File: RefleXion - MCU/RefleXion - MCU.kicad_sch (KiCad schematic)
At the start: 22 parts, among them J1 Conn_01x21, J2 USB_C_Receptacle_USB2.0, J3 Conn_01x01, J4 Conn_01x01, J5 Conn_01x21, J6 USB_C_Receptacle_USB2.0, Q1 AO3401A, U1 WeAct_Blackpill_v3_safepin, U2 SRV05-4, U3 74AHCT1G125

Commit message: fixes to RGB
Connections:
- no-connect marks 17 -> 19
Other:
- note added: "Left hand = R1 Right Hand = R2"
- note added: "RGB needs to be b9!"
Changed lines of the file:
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@@
   (no_connect (at 92.71 226.06))
   (no_connect (at 92.71 218.44))
+  (no_connect (at 191.77 245.11))
+  (no_connect (at 191.77 242.57))
   (wire (pts (xy 326.39 205.74) (xy 326.39 207.01))
     (stroke (width 0) (type default) (color 0 0 0 0))
@@
     (stroke (width 0) (type default) (color 0 0 0 0))
   )
+  (text "RGB needs to be b9!\n" (at 161.29 266.7 0)
+    (effects (font (size 1.27 1.27)) (justify left bottom))
+  )
+  (text "Left hand = R1\nRight Hand = R2" (at 337.82 201.93 0)
+    (effects (font (size 1.27 1.27)) (justify left bottom))
+  )
   (label "VBUS2" (at 118.11 213.36 0)

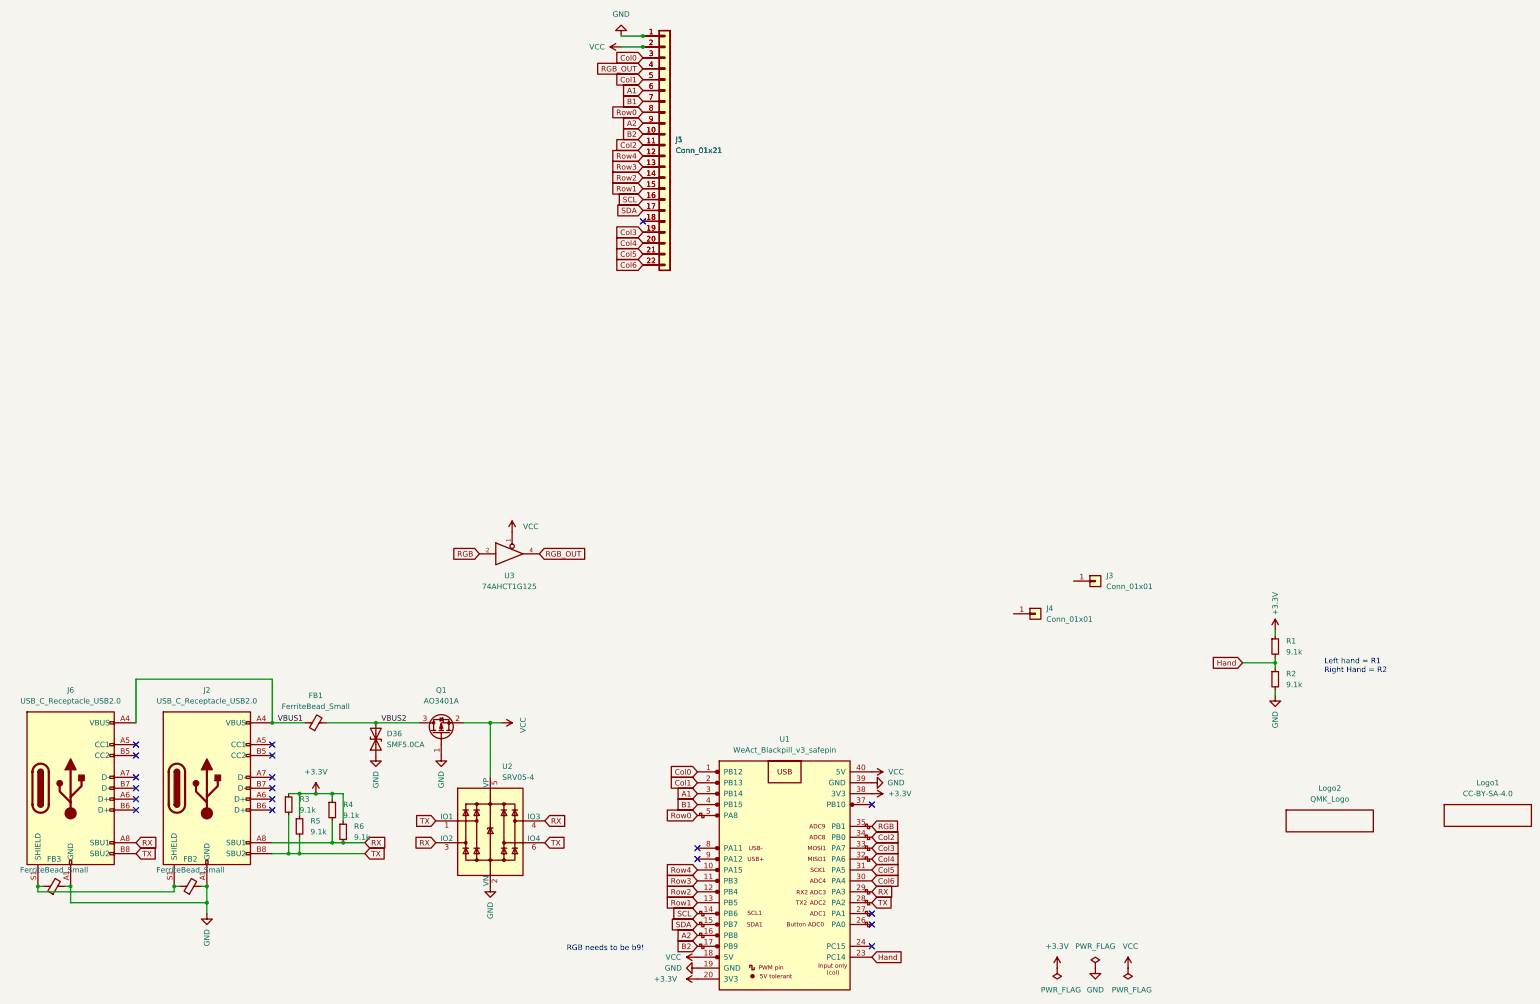
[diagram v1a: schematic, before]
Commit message: updated for RGB
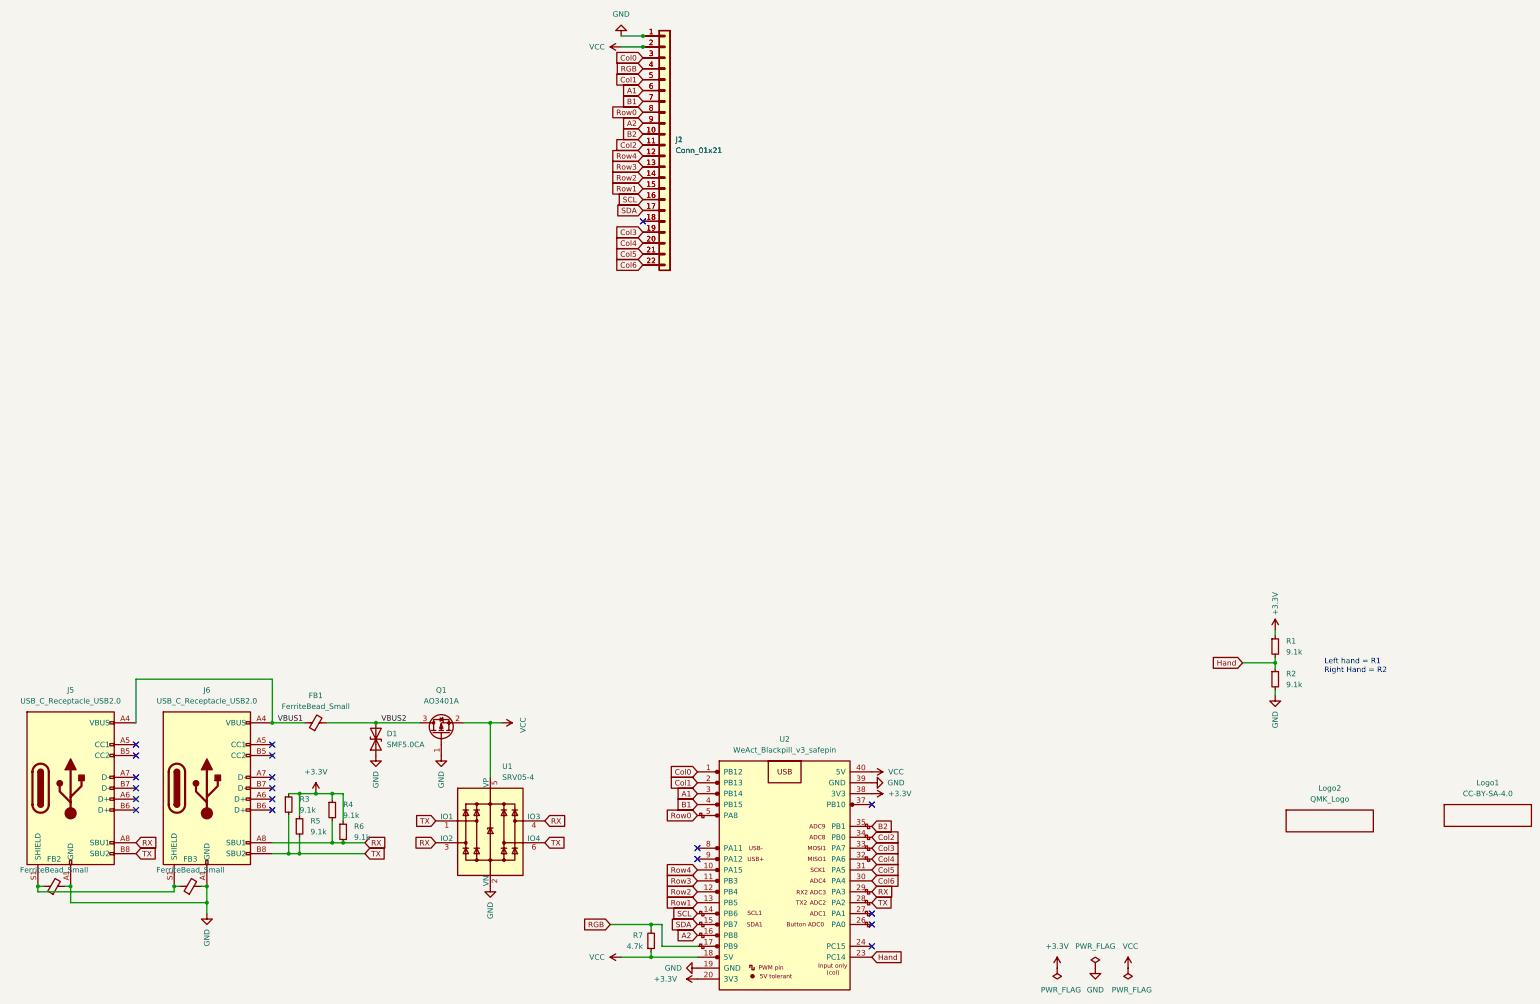
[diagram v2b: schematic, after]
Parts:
- removed J3, J4: Conn_01x01, Connector_PinHeader_2.54mm:PinHeader_1x01_P2.54mm_Vertical, symbol Connector_Generic:Conn_01x01
- removed U3: 74AHCT1G125, Package_TO_SOT_SMD:SOT-23-5_HandSoldering, symbol 74xGxx:74AHCT1G125
- added R7: 4.7k, Resistor_SMD:R_0603_1608Metric_Pad0.98x0.95mm_HandSolder, symbol Device:R_Small
- J5: renamed from J6; symbol Connector:USB_C_Receptacle_USB2.0 -> Keyboard Common:USB_C_Receptacle_USB2.0
- J6: renamed from J2; symbol Connector:USB_C_Receptacle_USB2.0 -> Keyboard Common:USB_C_Receptacle_USB2.0
- renumbered D36 to D1, FB3 to FB2, FB2 to FB3, J5 to J1, J1 to J2, U2 to U1, U1 to U2
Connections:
- net RGB_OUT is gone; now on net RGB: J1.4 (Pin_4), J2.4 (Pin_4)
- net B2: now also U2.35 (PB1); no longer U2.17 (PB9)
- net RGB: now also U2.17 (PB9), R7.2; no longer U2.35 (PB1)
- net VCC: now also R7.1
- net at FB2.1, FB3.1, J5.S1 (SHIELD)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: now also J5.S2 (SHIELD), J5.S3 (SHIELD), J5.S4 (SHIELD), J6.S2 (SHIELD), J6.S3 (SHIELD), J6.S4 (SHIELD)
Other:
- note removed: "RGB needs to be b9!"

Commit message: big dump
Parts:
- removed FB2: FerriteBead_Small, Capacitor_SMD:C_0805_2012Metric_Pad1.18x1.45mm_HandSolder, symbol Device:FerriteBead_Small
- removed R4, R5, R6: 9.1k, Resistor_SMD:R_0603_1608Metric_Pad0.98x0.95mm_HandSolder, symbol Device:R_Small
- removed R7: 4.7k, Resistor_SMD:R_0603_1608Metric_Pad0.98x0.95mm_HandSolder, symbol Device:R_Small
- J3: renamed from J5; symbol Keyboard Common:USB_C_Receptacle_USB2.0 -> Connector:USB_C_Receptacle_USB2.0
- J4: renamed from J6; symbol Keyboard Common:USB_C_Receptacle_USB2.0 -> Connector:USB_C_Receptacle_USB2.0
- renumbered FB3 to FB2, R3 to R1, R1 to R3
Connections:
- net +3.3V: no longer R1.1
- net B2: now also U2.17 (PB9); no longer U2.35 (PB1)
- net GND: now also FB2.1; no longer FB2.2
- net RGB: now also R1.2, U2.35 (PB1); no longer U2.17 (PB9)
- net RX: now also J3.B8 (SBU2); no longer J3.A8 (SBU1)
- net TX: now also J3.A8 (SBU1); no longer J3.B8 (SBU2), R1.2
- net VCC: now also R1.1
- new net SHIELD: FB2.2, J3.S1 (SHIELD), J4.S1 (SHIELD)
- no-connect marks 19 -> 17
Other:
- note added: "VCC = LEFT GND = RIGHT"
- note removed: "Left hand = R1 Right Hand = R2"
- moved on the sheet: FB2, R1
